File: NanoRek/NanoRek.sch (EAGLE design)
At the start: 13 parts

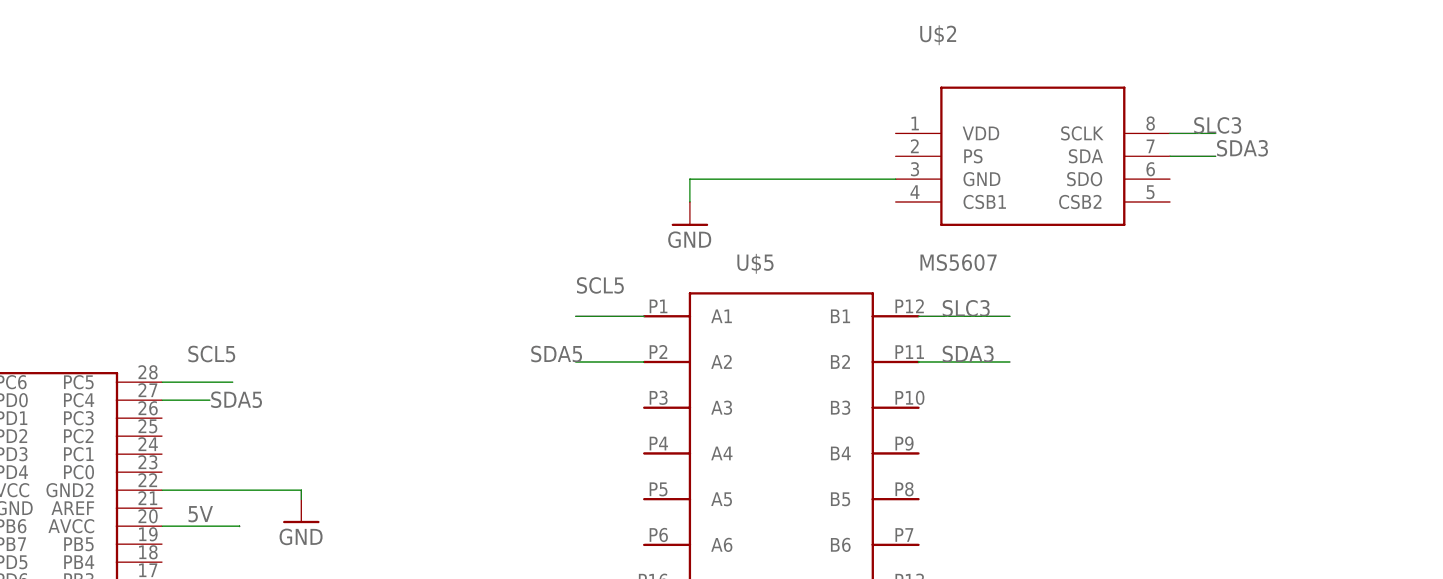
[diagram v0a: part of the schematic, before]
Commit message: Revert "Added I2C data line"
This reverts commit ce24847924fb5b1688f37034ce33982163fc9d56.
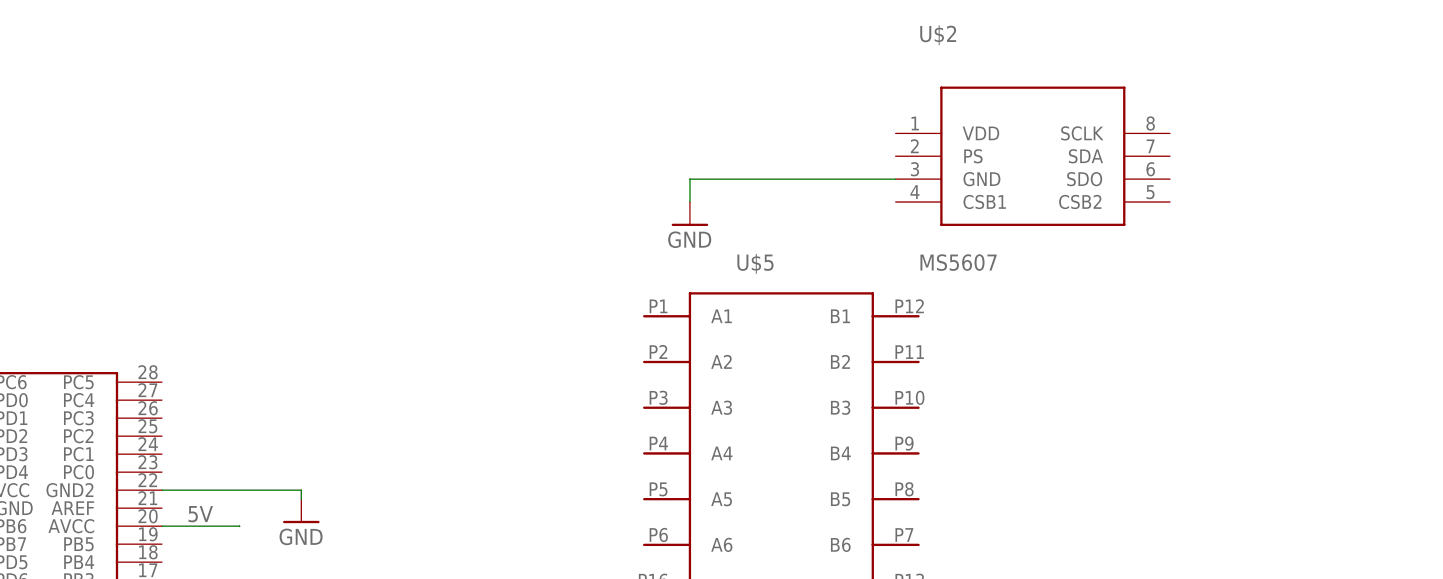
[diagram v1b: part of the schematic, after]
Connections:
- removed net SCL5: U$1.PC5, U$5.A1
- removed net SDA3: U$2.SDA, U$5.B2
- removed net SDA5: U$1.PC4, U$5.A2
- removed net SLC3: U$2.SCLK, U$5.B1
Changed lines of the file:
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@@
 <?xml version="1.0" encoding="utf-8"?>
 <!DOCTYPE eagle SYSTEM "eagle.dtd">
-<eagle version="8.3.2">
+<eagle version="8.4.0">
 <drawing>
 <settings>
@@
 </segment>
 </net>
-<net name="SDA5" class="0">
-<segment>
-<pinref part="U$1" gate="G$1" pin="PC4"/>
-<wire x1="86.12" y1="38.94" x2="91.44" y2="38.94" width="0.1524" layer="91"/>
-<label x="91.44" y="38.1" size="1.778" layer="95"/>
-</segment>
-<segment>
-<pinref part="U$5" gate="G$1" pin="A2"/>
-<wire x1="139.7" y1="43.18" x2="132.08" y2="43.18" width="0.1524" layer="91"/>
-<label x="127" y="43.18" size="1.778" layer="95"/>
-</segment>
-</net>
-<net name="SCL5" class="0">
-<segment>
-<pinref part="U$1" gate="G$1" pin="PC5"/>
-<wire x1="86.12" y1="40.94" x2="93.98" y2="40.94" width="0.1524" layer="91"/>
-<label x="88.9" y="43.18" size="1.778" layer="95"/>
-</segment>
-<segment>
-<pinref part="U$5" gate="G$1" pin="A1"/>
-<wire x1="139.7" y1="48.26" x2="132.08" y2="48.26" width="0.1524" layer="91"/>
-<label x="132.08" y="50.8" size="1.778" layer="95"/>
-</segment>
-</net>
-<net name="SLC3" class="0">
-<segment>
-<pinref part="U$5" gate="G$1" pin="B1"/>
-<wire x1="170.18" y1="48.26" x2="180.34" y2="48.26" width="0.1524" layer="91"/>
-<label x="172.72" y="48.26" size="1.778" layer="95"/>
-</segment>
-<segment>
-<pinref part="U$2" gate="G$1" pin="SCLK"/>
-<wire x1="198.12" y1="68.58" x2="203.2" y2="68.58" width="0.1524" layer="91"/>
-<label x="200.66" y="68.58" size="1.778" layer="95"/>
-</segment>
-</net>
-<net name="SDA3" class="0">
-<segment>
-<pinref part="U$5" gate="G$1" pin="B2"/>
-<wire x1="170.18" y1="43.18" x2="180.34" y2="43.18" width="0.1524" layer="91"/>
-<label x="172.72" y="43.18" size="1.778" layer="95"/>
-</segment>
-<segment>
-<pinref part="U$2" gate="G$1" pin="SDA"/>
-<wire x1="198.12" y1="66.04" x2="203.2" y2="66.04" width="0.1524" layer="91"/>
-<label x="203.2" y="66.04" size="1.778" layer="95"/>
-</segment>
-</net>
